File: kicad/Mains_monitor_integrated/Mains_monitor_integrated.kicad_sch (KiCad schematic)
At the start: 8 parts, among them J1 Conn_01x02_Pin, Q1 BS170, U1 HLW8032

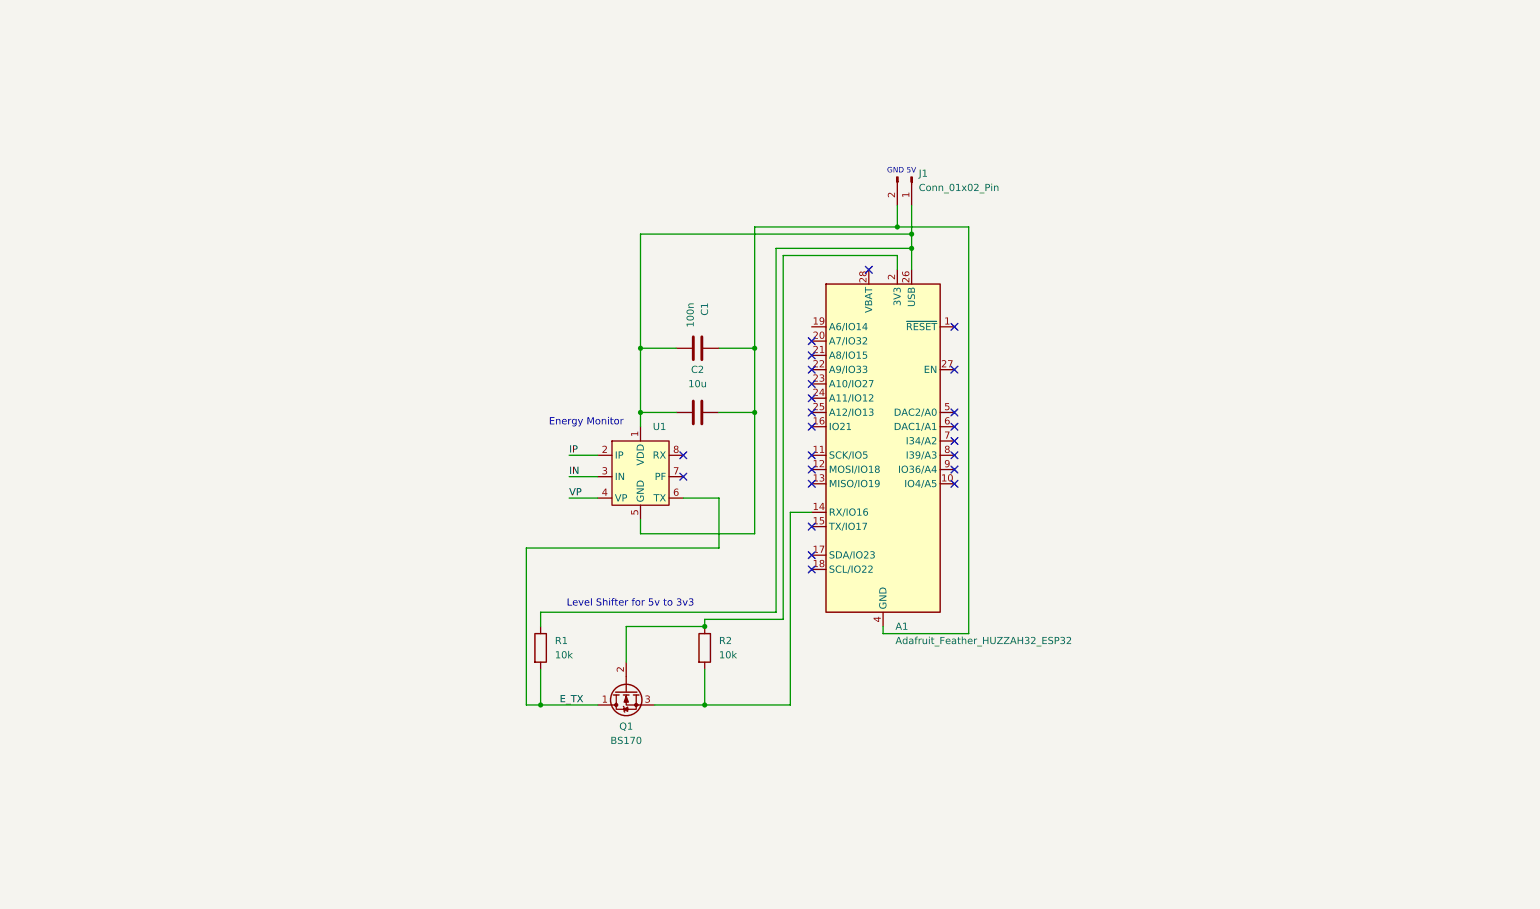
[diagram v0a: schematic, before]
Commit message: completed rough schematic and built first prototype pcb
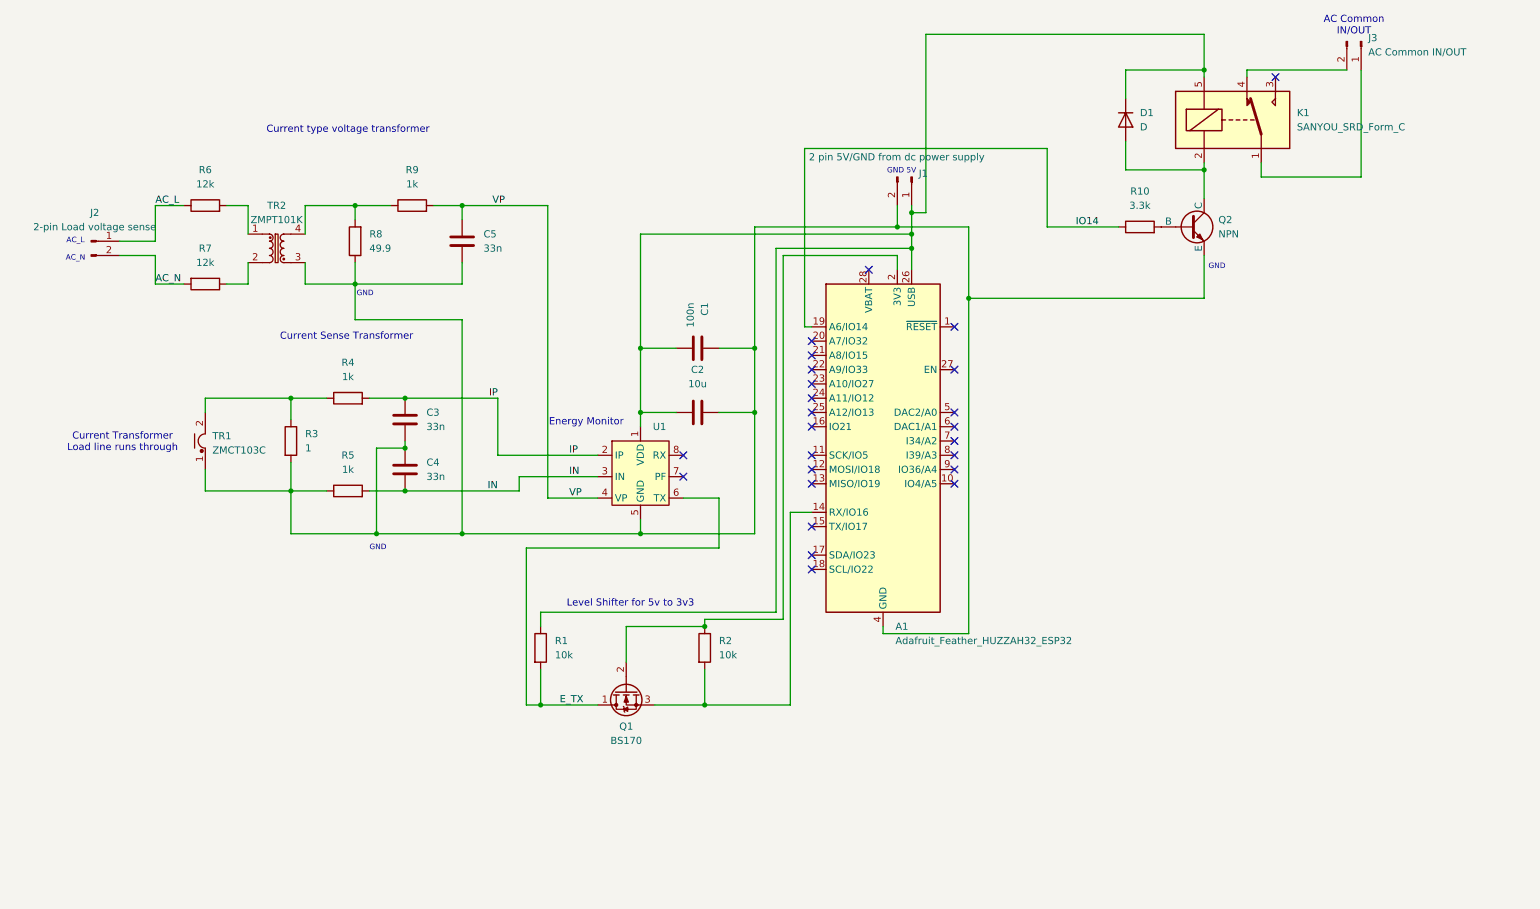
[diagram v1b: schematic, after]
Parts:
- added C3, C4, C5: 33n, Capacitor_SMD:C_0805_2012Metric_Pad1.18x1.45mm_HandSolder, symbol Device:C
- added D1: D, Diode_THT:D_5W_P10.16mm_Horizontal, symbol Device:D
- added J2: 2-pin Load voltage sense, Connector_PinHeader_2.54mm:PinHeader_1x02_P2.54mm_Vertical, symbol Connector:Conn_01x02_Pin
- added J3: AC Common IN/OUT, Connector_PinHeader_2.54mm:PinHeader_1x02_P2.54mm_Vertical, symbol Connector:Conn_01x02_Pin
- added K1: SANYOU_SRD_Form_C, Relay_THT:Relay_SPDT_SANYOU_SRD_Series_Form_C, symbol Relay:SANYOU_SRD_Form_C
- added Q2: NPN, Package_TO_SOT_THT:TO-92_Inline, symbol Simulation_SPICE:NPN
- added R10: 3.3k, Resistor_THT:R_Axial_DIN0414_L11.9mm_D4.5mm_P5.08mm_Vertical, symbol Device:R
- added R3: 1, Resistor_THT:R_Axial_DIN0414_L11.9mm_D4.5mm_P5.08mm_Vertical, symbol Device:R
- added R4, R5, R9: 1k, Resistor_THT:R_Axial_DIN0414_L11.9mm_D4.5mm_P5.08mm_Vertical, symbol Device:R
- added R6, R7: 12k, Resistor_THT:R_Axial_DIN0414_L11.9mm_D4.5mm_P5.08mm_Vertical, symbol Device:R
- added R8: 49.9, Resistor_THT:R_Axial_DIN0414_L11.9mm_D4.5mm_P5.08mm_Vertical, symbol Device:R
- added TR1: ZMCT103C, Transformer_THT:Transformer_Zeming_ZMCT103C, symbol Transformer:ZMCT103C
- added TR2: ZMPT101K, Transformer_THT:Transformer_Zeming_ZMPT101K, symbol Transformer:ZMPT101K
- J1: value Conn_01x02_Pin -> 2 pin 5V/GND from dc power supply; footprint (none) -> Connector_PinSocket_2.54mm:PinSocket_1x02_P2.54mm_Vertical
- R1, R2: footprint (none) -> Resistor_THT:R_Axial_DIN0414_L11.9mm_D4.5mm_P5.08mm_Vertical
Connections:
- net IN: now also C4.2, R5.2
- net IP: now also C3.1, R4.2
- net VP: now also C5.1, R9.2
- net IO14: now reaches A1.19 (A6/IO14)
- net IO14: now also R10.1
- net at A1.26 (USB), C1.2, C2.2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: now also D1.1 (K), K1.5
- net at A1.4 (GND), C1.1, C2.1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: now also C3.2, C4.1, C5.2, Q2.3 (E), R3.2, R5.1, R8.1, TR1.1, TR2.3
- new net: J3.1 (Pin_1), K1.1
- new net: D1.2 (A), K1.2, Q2.1 (C)
- new net: J3.2 (Pin_2), K1.4
- new net: Q2.2 (B), R10.2
- new net: R6.2, TR2.1
- new net: R7.1, TR2.2
- new net: R8.2, R9.1, TR2.4
- new net: R3.1, R4.1, TR1.2
- new net AC_L: J2.1 (Pin_1), R6.1
- new net AC_N: J2.2 (Pin_2), R7.2
- no-connect marks 24 -> 25
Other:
- note added: "AC Common IN/OUT"
- note added: "AC_L AC_N"
- note added: "Current Sense Transformer"
- note added: "Current Transformer Load line runs through"
- note added: "Current type voltage transformer"
- note added: "GND"

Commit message: Hello World
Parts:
- added C6: 100n, Capacitor_THT:C_Rect_L18.0mm_W5.0mm_P15.00mm_FKS3_FKP3, symbol Device:C
- added F1: 1.5A, symbol Device:Fuse
- added FL1: UU9.8N-103, Inductor_THT:Choke_Schaffner_RN102-04-14.0x14.0mm, symbol Filter:Choke_Schaffner_RN102-0.3-02-12M
- added J4: 120VAC, symbol Connector:Screw_Terminal_01x02
- added PS1: HLK-5M05, Converter_ACDC:Converter_ACDC_Hi-Link_HLK-5Mxx, symbol Converter_ACDC:HLK-5M05
- added RV1: 10D301K, symbol Device:Varistor
- added TH1: NTC10D-7, symbol Device:Thermistor_NTC
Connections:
- net AC_L: now also F1.1, J4.L (pin_2)
- net AC_N: now also C6.2, FL1.3, J4.N (Pin_1), RV1.2
- new net: FL1.1, TH1.2
- new net: FL1.2, PS1.1 (AC/L)
- new net: FL1.4, PS1.2 (AC/N)
- new net: C6.1, F1.2, RV1.1, TH1.1
- new net +5V: PS1.4 (+Vout)
- new net GND: PS1.3 (-Vout)
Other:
- moved on the sheet: A1, C1, C2, C3, C4, C5, D1, J1, J2, J3, K1, Q1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
